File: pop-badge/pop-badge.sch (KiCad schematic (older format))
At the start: 1 part, among them J1 Conn_01x04

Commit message: much more layouting
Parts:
- added H1, H2: MountingHole, MountingHole:MountingHole_4.3mm_M4, symbol Mechanical:MountingHole
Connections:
- net RGB LEDs/+5V renamed +5V
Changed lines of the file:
@@
 Wire Wire Line
 	2150 2450 1900 2450
+$Comp
+L Mechanical:MountingHole H1
+U 1 1 6190E265
+P 1500 5000
+F 0 "H1" H 1600 5046 50  0000 L CNN
+F 1 "MountingHole" H 1600 4955 50  0000 L CNN
+F 2 "MountingHole:MountingHole_4.3mm_M4" H 1500 5000 50  0001 C CNN
+F 3 "~" H 1500 5000 50  0001 C CNN
+	1    1500 5000
+	1    0    0    -1
+$EndComp
+$Comp
+L Mechanical:MountingHole H2
+U 1 1 6190E4B0
+P 1500 5300
+F 0 "H2" H 1600 5346 50  0000 L CNN
+F 1 "MountingHole" H 1600 5255 50  0000 L CNN
+F 2 "MountingHole:MountingHole_4.3mm_M4" H 1500 5300 50  0001 C CNN
+F 3 "~" H 1500 5300 50  0001 C CNN
+	1    1500 5300
+	1    0    0    -1
+$EndComp
+Text Label 2150 2450 0    50   ~ 0
++5V
 $EndSCHEMATC

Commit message: routing done
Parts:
- added U26: Pico, RPi_Pico:RPi_Pico_SMD, symbol RPi-Pico:Pico
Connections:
- net +5V: now also U26.39 (VSYS)
- net RGB LEDs/DIN renamed DIN
- net DIN: now also U26.34 (GPIO28_ADC2)
- net RGB LEDs/GND renamed GND
- net GND: now also U26.3 (GND)
- net White LEDs/LEDwMCU renamed LEDwMCU
- net LEDwMCU: now also U26.29 (GPIO22)
- no-connect marks 0 -> 39
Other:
- moved on the sheet: J1
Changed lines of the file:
@@
 Comment4 ""
 $EndDescr
-Wire Wire Line
-	2150 2500 2300 2500
-Wire Wire Line
-	2550 2550 2450 2550
-Wire Wire Line
-	2450 2550 2450 2500
-$Sheet
-S 1350 3250 550  550
-U 615492B8
-F0 "White LEDs" 50
-F1 "white-leds.sch" 50
-F2 "LEDwMCU" I R 1900 3550 50
-F3 "GND" I R 1900 3700 50
-F4 "+5V" I R 1900 3400 50
-$EndSheet
 $Comp
 L Connector_Generic:Conn_01x04 J1
 U 1 1 6163BF0A
-P 2750 2650
-F 0 "J1" H 2830 2642 50  0000 L CNN
-F 1 "Conn_01x04" H 2830 2551 50  0000 L CNN
-F 2 "Connector_PinHeader_1.27mm:PinHeader_1x04_P1.27mm_Vertical" H 2750 2650 50  0001 C CNN
-F 3 "~" H 2750 2650 50  0001 C CNN
-	1    2750 2650
+P 1600 850
+F 0 "J1" H 1680 842 50  0000 L CNN
+F 1 "Conn_01x04" H 1680 751 50  0000 L CNN
+F 2 "Connector_PinHeader_1.27mm:PinHeader_1x04_P1.27mm_Vertical" H 1600 850 50  0001 C CNN
+F 3 "~" H 1600 850 50  0001 C CNN
+	1    1600 850
 	1    0    0    -1
 $EndComp
-Wire Wire Line
-	2550 2750 2400 2750
-Wire Wire Line
-	2450 2850 2550 2850
-Wire Wire Line
-	2450 2850 2450 3550
-Wire Wire Line
-	1900 3550 2450 3550
-Wire Wire Line
-	1900 3700 2400 3700
-Connection ~ 2400 2750
-Wire Wire Line
-	2400 2750 2150 2750
-Wire Wire Line
-	2400 3700 2400 2750
-Wire Wire Line
-	2300 2500 2300 3400
-Wire Wire Line
-	2300 3400 1900 3400
-Connection ~ 2300 2500
-Wire Wire Line
-	2300 2500 2450 2500
 $Sheet
 S 1100 2350 800  650
@@
 F4 "DIN" I R 1900 2650 50
 $EndSheet
-Wire Wire Line
-	2150 2750 2150 2850
-Wire Wire Line
-	2150 2850 1900 2850
-Wire Wire Line
-	1900 2650 2550 2650
-Wire Wire Line
-	2150 2500 2150 2450
-Wire Wire Line
-	2150 2450 1900 2450
 $Comp
 L Mechanical:MountingHole H1
@@
 	1    0    0    -1
 $EndComp
-Text Label 2150 2450 0    50   ~ 0
+$Comp
+L RPi-Pico:Pico U26
+U 1 1 61A68EB5
+P 4150 1800
+F 0 "U26" H 4150 3015 50  0000 C CNN
+F 1 "Pico" H 4150 2924 50  0000 C CNN
+F 2 "RPi_Pico:RPi_Pico_SMD" V 4150 1800 50  0001 C CNN
+F 3 "" H 4150 1800 50  0001 C CNN
+	1    4150 1800
+	1    0    0    -1
+$EndComp
+NoConn ~ 4050 2950
+NoConn ~ 4150 2950
+NoConn ~ 4250 2950
+NoConn ~ 4850 2650
+NoConn ~ 4850 2550
+NoConn ~ 4850 2450
+NoConn ~ 4850 2350
+NoConn ~ 4850 2250
+NoConn ~ 4850 2150
+NoConn ~ 4850 2050
+NoConn ~ 4850 2750
+NoConn ~ 4850 1850
+NoConn ~ 4850 1750
+NoConn ~ 4850 1650
+NoConn ~ 4850 1550
+NoConn ~ 4850 1350
+NoConn ~ 4850 1250
+NoConn ~ 4850 1150
+NoConn ~ 4850 1050
+NoConn ~ 4850 850
+NoConn ~ 3450 850
+NoConn ~ 3450 950
+NoConn ~ 3450 1150
+NoConn ~ 3450 1250
+NoConn ~ 3450 1350
+NoConn ~ 3450 1450
+NoConn ~ 3450 1550
+NoConn ~ 3450 1650
+NoConn ~ 3450 1750
+NoConn ~ 3450 1850
+NoConn ~ 3450 1950
+NoConn ~ 3450 2050
+NoConn ~ 3450 2150
+NoConn ~ 3450 2250
+NoConn ~ 3450 2350
+NoConn ~ 3450 2450
+NoConn ~ 3450 2550
+NoConn ~ 3450 2650
+NoConn ~ 3450 2750
+Text GLabel 1200 1050 0    50   Input ~ 0
+LEDwMCU
+Text GLabel 5100 950  2    50   Input ~ 0
 +5V
+Text GLabel 5100 1450 2    50   Input ~ 0
+DIN
+Text GLabel 3200 1050 0    50   Input ~ 0
+GND
+$Sheet
+S 1350 3250 550  550
+U 615492B8
+F0 "White LEDs" 50
+F1 "white-leds.sch" 50
+F2 "LEDwMCU" I R 1900 3550 50
+F3 "GND" I R 1900 3700 50
+F4 "+5V" I R 1900 3400 50
+$EndSheet
+Wire Wire Line
+	1400 1050 1200 1050
+Wire Wire Line
+	3200 1050 3450 1050
+Wire Wire Line
+	4850 1450 5100 1450
+Wire Wire Line
+	5100 950  4850 950
+Text GLabel 2150 3400 2    50   Input ~ 0
++5V
+Text GLabel 2150 3550 2    50   Input ~ 0
+LEDwMCU
+Text GLabel 2150 3700 2    50   Input ~ 0
+GND
+Wire Wire Line
+	2150 3700 1900 3700
+Wire Wire Line
+	1900 3550 2150 3550
+Wire Wire Line
+	2150 3400 1900 3400
+Text GLabel 5100 1950 2    50   Input ~ 0
+LEDwMCU
+Wire Wire Line
+	5100 1950 4850 1950
+Wire Wire Line
+	1200 950  1400 950
+Wire Wire Line
+	1400 850  1200 850
+Wire Wire Line
+	1200 750  1400 750
+Text GLabel 1200 950  0    50   Input ~ 0
+GND
+Text GLabel 1200 850  0    50   Input ~ 0
+DIN
+Text GLabel 1200 750  0    50   Input ~ 0
++5V
+Text GLabel 2100 2450 2    50   Input ~ 0
++5V
+Text GLabel 2100 2650 2    50   Input ~ 0
+DIN
+Text GLabel 2100 2850 2    50   Input ~ 0
+GND
+Wire Wire Line
+	2100 2450 1900 2450
+Wire Wire Line
+	1900 2650 2100 2650
+Wire Wire Line
+	2100 2850 1900 2850
 $EndSCHEMATC

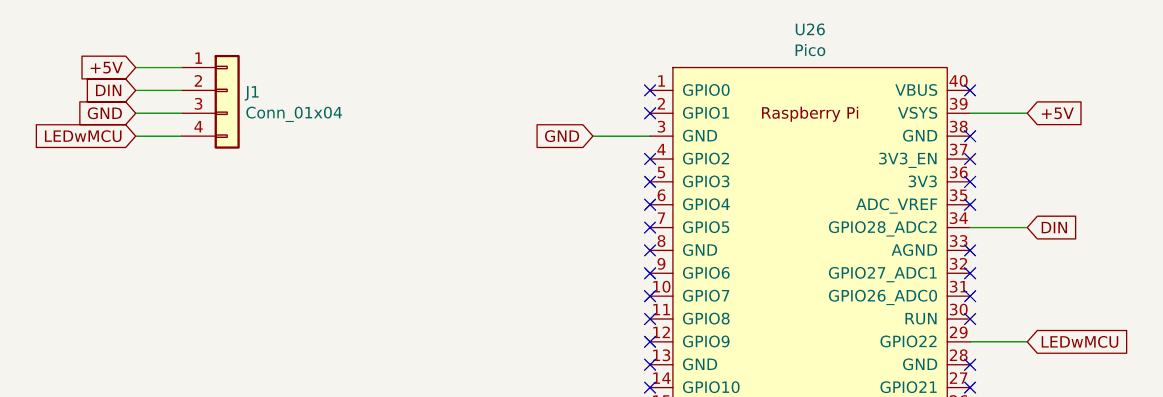
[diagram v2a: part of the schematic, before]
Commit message: redo power rails to avoid loops
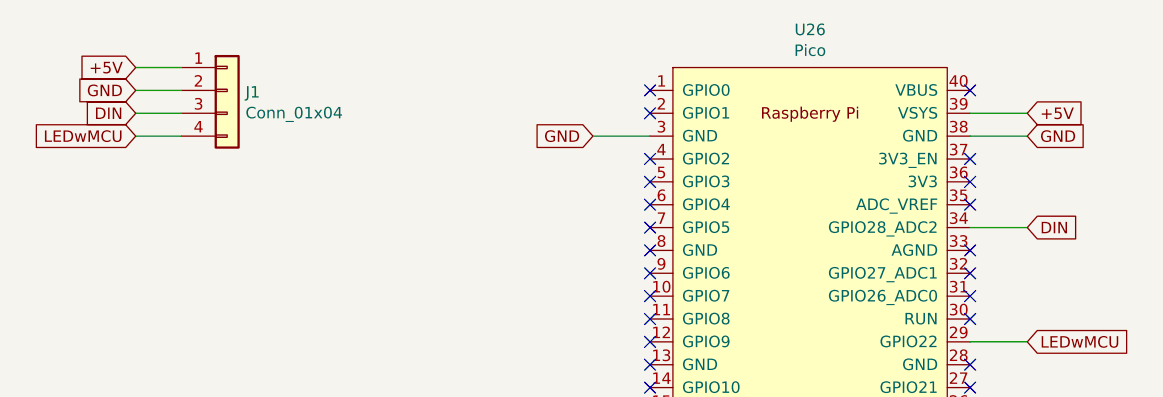
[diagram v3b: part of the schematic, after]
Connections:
- net DIN: now also J1.3 (Pin_3); no longer J1.2 (Pin_2)
- net GND: now also J1.2 (Pin_2), U26.38 (GND); no longer J1.3 (Pin_3)
- no-connect marks 39 -> 38
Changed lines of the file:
@@
 NoConn ~ 4850 1250
 NoConn ~ 4850 1150
-NoConn ~ 4850 1050
 NoConn ~ 4850 850
 NoConn ~ 3450 850
@@
 Text GLabel 5100 1450 2    50   Input ~ 0
 DIN
-Text GLabel 3200 1050 0    50   Input ~ 0
-GND
 $Sheet
 S 1350 3250 550  550
@@
 	5100 1950 4850 1950
 Wire Wire Line
-	1200 950  1400 950
-Wire Wire Line
-	1400 850  1200 850
-Wire Wire Line
 	1200 750  1400 750
-Text GLabel 1200 950  0    50   Input ~ 0
-GND
-Text GLabel 1200 850  0    50   Input ~ 0
-DIN
 Text GLabel 1200 750  0    50   Input ~ 0
 +5V
@@
 Wire Wire Line
 	2100 2850 1900 2850
+Text GLabel 3200 1050 0    50   Input ~ 0
+GND
+Wire Wire Line
+	1200 850  1400 850
+Text GLabel 1200 850  0    50   Input ~ 0
+GND
+Wire Wire Line
+	1400 950  1200 950
+Text GLabel 1200 950  0    50   Input ~ 0
+DIN
+Wire Wire Line
+	5100 1050 4850 1050
+Text GLabel 5100 1050 2    50   Input ~ 0
+GND
 $EndSCHEMATC

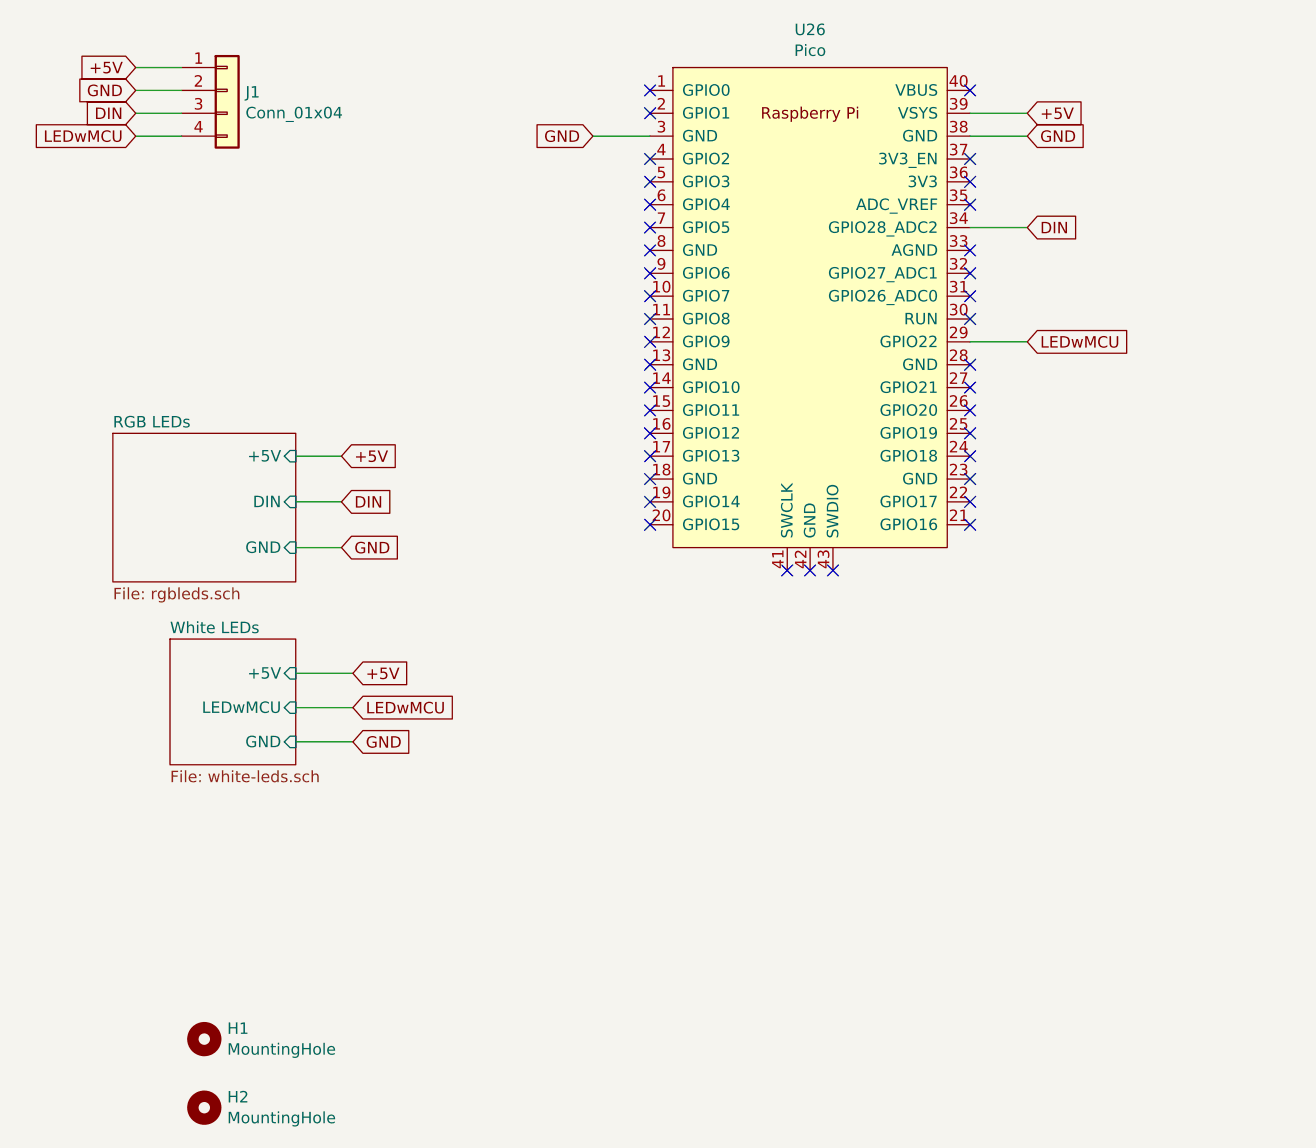
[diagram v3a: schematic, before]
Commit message: use proper pin connector and expose LEDw- on connector
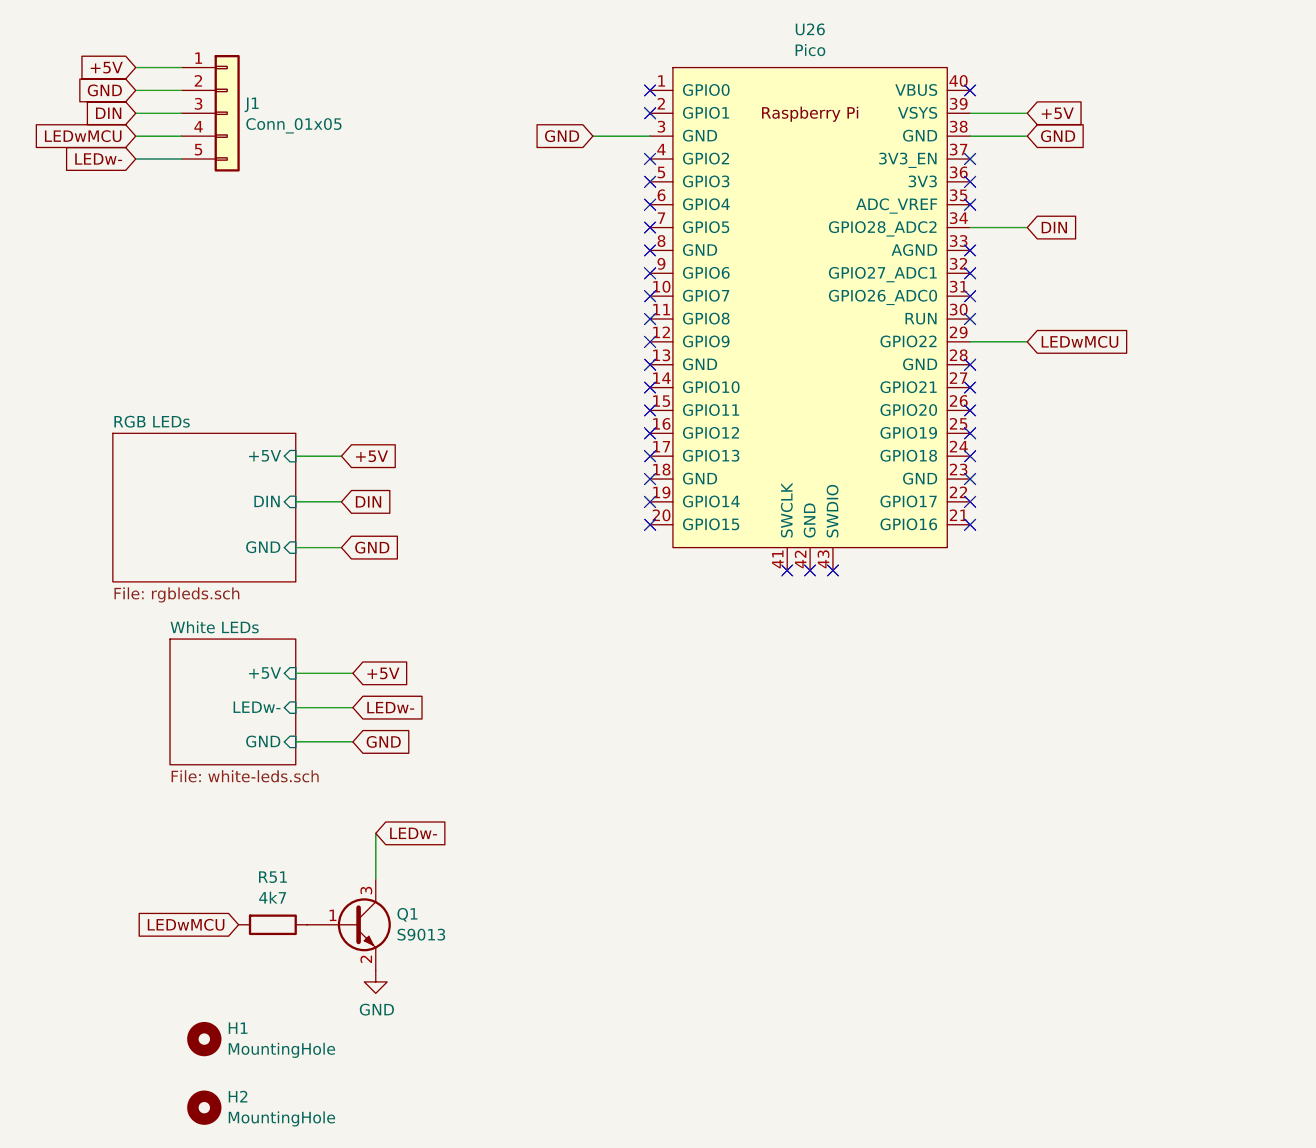
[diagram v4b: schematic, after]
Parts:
- removed J1: Conn_01x04, Connector_PinHeader_1.27mm:PinHeader_1x04_P1.27mm_Vertical, symbol Connector_Generic:Conn_01x04
- added J1: Conn_01x05, Connector_PinSocket_2.54mm:PinSocket_1x05_P2.54mm_Vertical, symbol Connector_Generic:Conn_01x05
- added Q1: S9013, Package_TO_SOT_SMD:SOT-23, symbol Transistor_BJT:BC818
- added R51: 4k7, Resistor_SMD:R_0603_1608Metric_Pad1.05x0.95mm_HandSolder, symbol Device:R
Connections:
- net +5V: now also J1.1 (Pin_1)
- net DIN: now also J1.3 (Pin_3)
- net GND: now also J1.2 (Pin_2), Q1.2 (E)
- net LEDwMCU: now also J1.4 (Pin_4), R51.2
- new net: Q1.1 (B), R51.1
- new net LEDw-: J1.5 (Pin_5), Q1.3 (C)
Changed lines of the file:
@@
 Comment4 ""
 $EndDescr
-$Comp
-L Connector_Generic:Conn_01x04 J1
-U 1 1 6163BF0A
-P 1600 850
-F 0 "J1" H 1680 842 50  0000 L CNN
-F 1 "Conn_01x04" H 1680 751 50  0000 L CNN
-F 2 "Connector_PinHeader_1.27mm:PinHeader_1x04_P1.27mm_Vertical" H 1600 850 50  0001 C CNN
-F 3 "~" H 1600 850 50  0001 C CNN
-	1    1600 850
-	1    0    0    -1
-$EndComp
 $Sheet
 S 1100 2350 800  650
@@
 F0 "White LEDs" 50
 F1 "white-leds.sch" 50
-F2 "LEDwMCU" I R 1900 3550 50
-F3 "GND" I R 1900 3700 50
-F4 "+5V" I R 1900 3400 50
+F2 "GND" I R 1900 3700 50
+F3 "+5V" I R 1900 3400 50
+F4 "LEDw-" I R 1900 3550 50
 $EndSheet
 Wire Wire Line
@@
 Text GLabel 2150 3400 2    50   Input ~ 0
 +5V
-Text GLabel 2150 3550 2    50   Input ~ 0
+Text GLabel 1650 4500 0    50   Input ~ 0
 LEDwMCU
 Text GLabel 2150 3700 2    50   Input ~ 0
@@
 Text GLabel 5100 1050 2    50   Input ~ 0
 GND
+$Comp
+L Device:R R?
+U 1 1 61BDB595
+P 1800 4500
+AR Path="/615492B8/61BDB595" Ref="R?"  Part="1"
+AR Path="/61BDB595" Ref="R51"  Part="1"
+F 0 "R51" V 1593 4500 50  0000 C CNN
+F 1 "4k7" V 1684 4500 50  0000 C CNN
+F 2 "Resistor_SMD:R_0603_1608Metric_Pad1.05x0.95mm_HandSolder" V 1730 4500 50  0001 C CNN
+F 3 "~" H 1800 4500 50  0001 C CNN
+F 4 "0603" H 1800 4500 50  0001 C CNN "JLC"
+	1    1800 4500
+	0    1    1    0
+$EndComp
+Wire Wire Line
+	2250 4100 2250 4300
+$Comp
+L Transistor_BJT:BC818 Q?
+U 1 1 61BDB59D
+P 2150 4500
+AR Path="/615492B8/61BDB59D" Ref="Q?"  Part="1"
+AR Path="/61BDB59D" Ref="Q1"  Part="1"
+F 0 "Q1" H 2341 4546 50  0000 L CNN
+F 1 "S9013" H 2341 4455 50  0000 L CNN
+F 2 "Package_TO_SOT_SMD:SOT-23" H 2350 4425 50  0001 L CIN
+F 3 "" H 2150 4500 50  0001 L CNN
+F 4 "C6749" H 2150 4500 50  0001 C CNN "JLC"
+	1    2150 4500
+	1    0    0    -1
+$EndComp
+$Comp
+L power:GND #PWR053
+U 1 1 61BDD33B
+P 2250 4700
+F 0 "#PWR053" H 2250 4450 50  0001 C CNN
+F 1 "GND" H 2255 4527 50  0000 C CNN
+F 2 "" H 2250 4700 50  0001 C CNN
+F 3 "" H 2250 4700 50  0001 C CNN
+	1    2250 4700
+	1    0    0    -1
+$EndComp
+Text GLabel 2150 3550 2    50   Input ~ 0
+LEDw-
+Text GLabel 2250 4100 2    50   Input ~ 0
+LEDw-
+$Comp
+L Connector_Generic:Conn_01x05 J1
+U 1 1 61BFACBB
+P 1600 950
+F 0 "J1" H 1680 992 50  0000 L CNN
+F 1 "Conn_01x05" H 1680 901 50  0000 L CNN
+F 2 "Connector_PinSocket_2.54mm:PinSocket_1x05_P2.54mm_Vertical" H 1600 950 50  0001 C CNN
+F 3 "~" H 1600 950 50  0001 C CNN
+	1    1600 950
+	1    0    0    -1
+$EndComp
+Text GLabel 1200 1150 0    50   Input ~ 0
+LEDw-
+Wire Wire Line
+	1200 1150 1400 1150
 $EndSCHEMATC
